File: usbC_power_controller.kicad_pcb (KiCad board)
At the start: 2 copper layers, 22.5 x 37.5 mm, 9 parts, among them J1 Conn_Coaxial, J3 Conn_01x02_Pin, J4 USB_A_Stacked, J5 Conn_01x02_Pin, Q1 AO3400A, U1 EL817

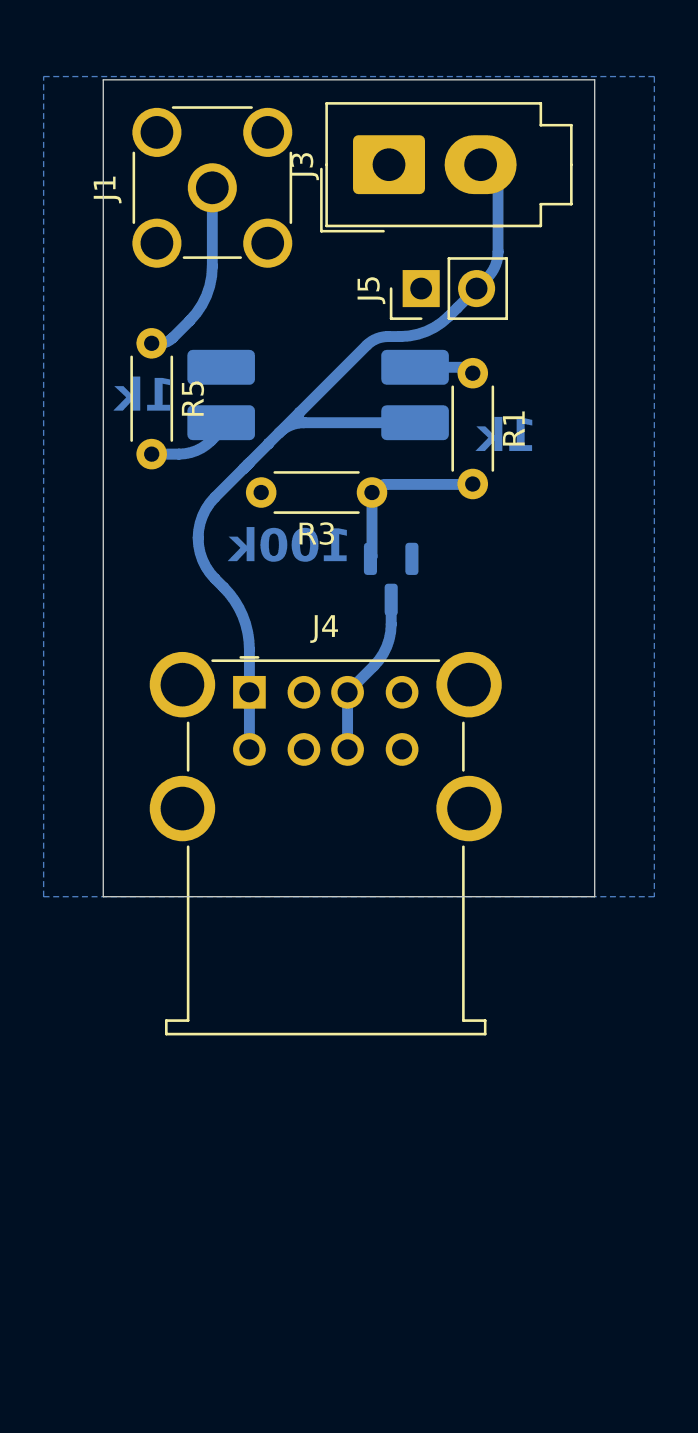
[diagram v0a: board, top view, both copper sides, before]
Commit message: updated power distribution board
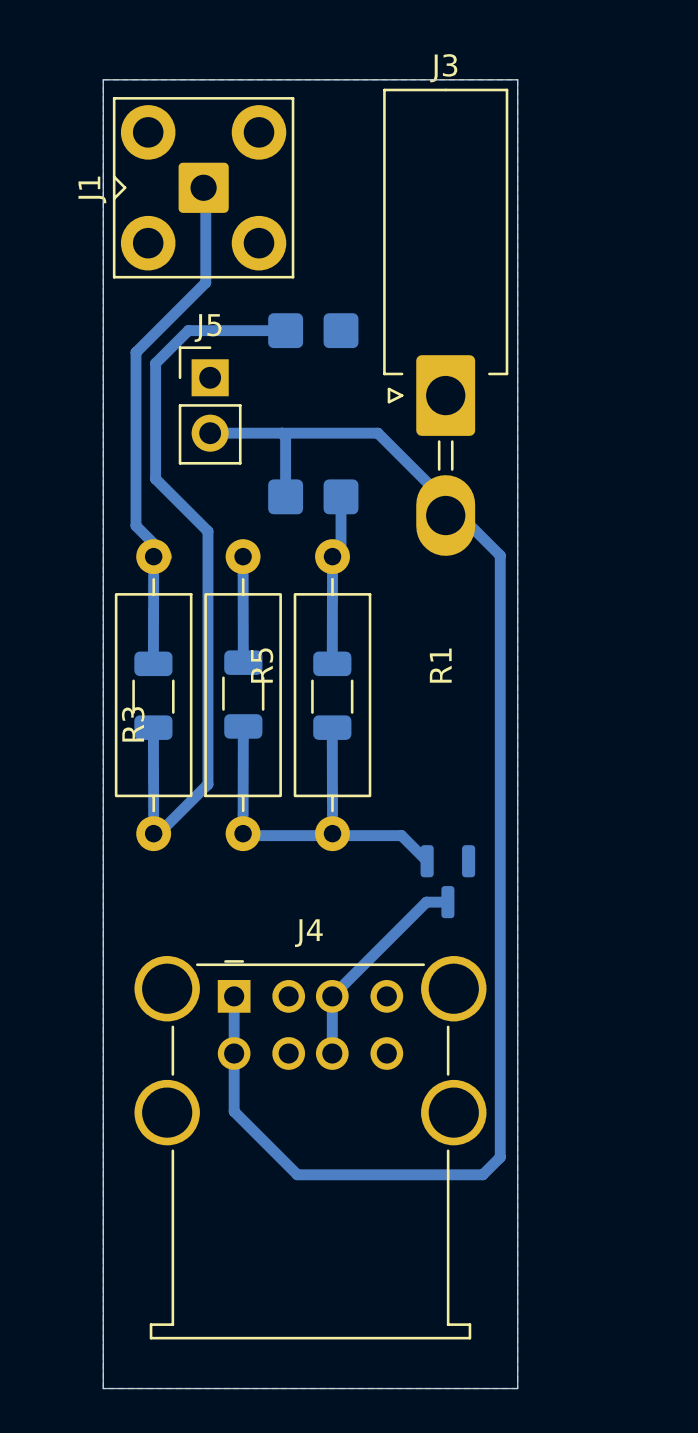
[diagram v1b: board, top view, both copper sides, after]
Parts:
- J1: footprint Connector_Coaxial:SMA_Molex_73251-2200_Horizontal -> SMA:SMA_Amphenol_901-143_Horizontal
- J3: footprint Trodes_SMA:Molex_Mini-Fit_Jr_5566-02A_2x01_P4.20mm_Vertical -> SMA:Molex_Mini-Fit_Jr_5569-02A2_2x01_P4.20mm_Horizontal
- J4: footprint Trodes_SMA:USB_A_Wuerth_61400826021_Horizontal_Stacked -> Connector_USB:USB_A_Wuerth_61400826021_Horizontal_Stacked
- R1, R3, R5: footprint Resistor_THT:R_Axial_DIN0204_L3.6mm_D1.6mm_P5.08mm_Horizontal -> SMA:R_tht1270_smd3216
- U1: footprint Package_DIP:DIP-4_W8.89mm_SMDSocket_LongPads -> Package_DIP:DIP-4_W7.62mm_SMDSocket_SmallPads
- moved R3 16.7 mm to (130.3, 106.6), turned to 90 degrees
- moved Q1 14.1 mm to (139.7, 108.8)
- moved J4 14.0 mm to (129.9, 114.0)
- moved J3 11.0 mm to (139.6, 86.5), turned to 0 degrees
- moved R1 10.6 mm to (134.4, 93.9)
- moved J5 10.5 mm to (128.8, 85.7), turned to 0 degrees
- moved R5 9.78 mm to (126.2, 93.9)
- moved U1 0.89 mm to (133.5, 87.3), turned to -90 degrees
- moved J1 0.40 mm to (128.5, 76.9)
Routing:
- net Net-(R5-Pad2): track 3.74 -> 30.3 mm
- net VCC: track 41.6 -> 65.2 mm
- net Net-(J1-In): track 8.49 -> 18.9 mm
- net /illumination: track 7.56 -> 9.71 mm
- net Net-(Q1-G): track 7.78 -> 8.36 mm
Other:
- board size 22.5 x 37.5 mm -> 19 x 60 mm
- board text removed: "100k"
- board text removed: "1k"
